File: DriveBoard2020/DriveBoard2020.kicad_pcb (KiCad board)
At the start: 2 copper layers, 124.5 x 107.4 mm, 92 parts, among them SW0 SW_SPST, SW1 SW_Push, SW2 SW_Push, SW3 SW_Push, SW4 SW_Push, SW5 SW_Push, SW6 SW_Push, SW7 SW_Push, SW8 SW_Push, SW9 SW_Push, U1 MAX_3232, U2 MAX_3232, U3 OKI, U4 TM4C129E_Launchpad, U5 MAX_3232, U6 OKI, U8 LDD-1500L

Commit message: finished schematic
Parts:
- removed Conn8: AndersonPP, MRDT_Connectors:Anderson_2_Horizontal_Side_by_Side
- Conn10: value Molex_SL_02 -> Molex_SL_04; footprint MRDT_Connectors:MOLEX_SL_02_Horizontal -> MRDT_Connectors:MOLEX_SL_04_Horizontal
- moved D22 242.8 mm to (220.1, 2.40)
- moved D23 239.8 mm to (209.9, 2.40)
- moved D20 239.3 mm to (204.9, 2.54)
- moved D15 239.2 mm to (200.0, 2.40)
- moved D21 238.2 mm to (189.6, 2.54)
- moved R24 226.6 mm to (189.6, 0.00)
- moved D12 176.3 mm to (128.7, 40.6)
- moved R26 143.4 mm to (209.9, 5.08)
- moved R23 138.0 mm to (204.9, 5.08)
- moved R10 134.2 mm to (123.6, 27.9)
- moved R25 132.3 mm to (220.1, 5.08)
- moved Conn10 130.2 mm to (242.6, 86.4)
- moved D10 128.3 mm to (128.7, 27.9)
- moved SW2 127.4 mm to (127.0, 22.9)
- moved R12 125.4 mm to (123.6, 40.6)
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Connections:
- net Net-(U4-PadPD0) renamed MISO2
- net Net-(U4-PadPD1) renamed MOSI2
- net Net-(U4-PadPD2) renamed cs2
- net Net-(U4-PadPD3) renamed clk2
- Conn10 pad 1: /Headlight_V1+ -> Net-(Conn10-Pad1)
- Conn10 pad 2: /Headlight_V1- -> Net-(Conn10-Pad2)
- U4 pad PF1: Net-(U4-PadPF1) -> Headlight_OnOff_PWM
- U4 pad PK5: Net-(U4-PadPK5) -> FL_Motor
- U4 pad PK6: Net-(U4-PadPK6) -> RL_Motor
- U4 pad PM2: Net-(U4-PadPM2) -> ML_Motor
- U8 pad 11: /Headlight_V1- -> Net-(Conn10-Pad2)
- U8 pad 12: /Headlight_V1- -> Net-(Conn10-Pad2)
- U8 pad 13: /Headlight_V1+ -> Net-(Conn10-Pad1)
- U8 pad 14: /Headlight_V1+ -> Net-(Conn10-Pad1)
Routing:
- added copper zone on B.Cu, net GND
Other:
- board outline removed

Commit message: layout progress
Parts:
- removed D15, D3, D5, D6: LED, LED_SMD:LED_0603_1608Metric_Pad1.05x0.95mm_HandSolder
- added Rx3: LED, LED_SMD:LED_0603_1608Metric_Pad1.05x0.95mm_HandSolder, F.Cu at (161.7, 85.1)
- added Tx3: LED, LED_SMD:LED_0603_1608Metric_Pad1.05x0.95mm_HandSolder, F.Cu at (165.4, 85.1)
- added Tx4: LED, LED_SMD:LED_0603_1608Metric_Pad1.05x0.95mm_HandSolder, F.Cu at (156.6, 85.1)
- added Tx7: LED, LED_SMD:LED_0603_1608Metric_Pad1.05x0.95mm_HandSolder, F.Cu at (130.2, 85.1)
- Change Direction: renamed from SW0
- Front Left Motor: renamed from SW2
- Front Right Motor: renamed from SW1
- Middle Left Motor: renamed from SW4
- Middle Right Motor: renamed from SW3
- Neopixel Pattern: renamed from SW9
- Neopixel White: renamed from SW8
- Rear Left Motor: renamed from SW6
- Rear Right Motor: renamed from SW5
- moved U2 151.7 mm to (269.9, 152.4)
- moved U5 150.8 mm to (269.9, 180.3)
- moved U1 150.2 mm to (269.9, 166.4)
- moved U6 129.1 mm to (154.9, 141.0), turned to 90 degrees
- moved C4 127.5 mm to (263.5, 170.8), turned to 90 degrees
- moved U3 124.7 mm to (154.9, 153.7), turned to 90 degrees
- moved C5 123.2 mm to (263.5, 186.1), turned to 270 degrees
- moved C6 111.7 mm to (263.5, 146.4), turned to 270 degrees
- moved C7 107.6 mm to (263.5, 151.1), turned to 270 degrees
- moved R18 107.5 mm to (130.2, 87.0)
- moved C8 104.5 mm to (263.5, 161.9), turned to 270 degrees
- moved R22 103.8 mm to (126.4, 87.0)
- moved U8 103.2 mm to (197.5, 130.8)
- moved Tx6 102.6 mm to (139.1, 85.1), turned to 0 degrees
- moved R1 102.3 mm to (139.1, 87.0), turned to 0 degrees
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- renumbered SW7 to Headlights, D23 to Rx2, D4 to Rx4, D21 to Rx5, D2 to Rx6, D19 to Rx7, D22 to Tx2, D20 to Tx5, D1 to Tx6
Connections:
- Conn1 pad 3: (no net) -> +12VA
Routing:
- net +12VA: track 0.00 -> 50.2 mm
- net +12V: track 0.00 -> 27.7 mm
- net Net-(C3-Pad1): track 0.00 -> 22.8 mm
- net Net-(C4-Pad1): track 0.00 -> 21.6 mm
- net Net-(C5-Pad1): track 0.00 -> 20.2 mm
- net Net-(C5-Pad2): track 0.00 -> 7.26 mm
- net Net-(C6-Pad2): track 0.00 -> 5.19 mm
- net Net-(C6-Pad1): track 0.00 -> 4.86 mm
- net Net-(C8-Pad2): track 0.00 -> 4.56 mm
- net Net-(C4-Pad2): track 0.00 -> 4.56 mm
- net Net-(C7-Pad1): track 0.00 -> 4.50 mm
- net Net-(C13-Pad2): track 0.00 -> 4.40 mm
- net Net-(C7-Pad2): track 0.00 -> 4.30 mm
- net Net-(C8-Pad1): track 0.00 -> 4.24 mm
- net Net-(C13-Pad1): track 0.00 -> 4.20 mm
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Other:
- board text added: "MOTORS"
- board text added: "Power Indicators"
- board text added: "Serial Indicators"

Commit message: working on traces
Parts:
- removed Change Direction: SW_SPST, Button_Switch_THT:SW_CuK_JS202011AQN_DPDT_Angled
- removed D17, D18: Org_LED, LED_SMD:LED_0603_1608Metric_Pad1.05x0.95mm_HandSolder
- removed R20, R21: 500, Resistor_SMD:R_0603_1608Metric_Pad1.05x0.95mm_HandSolder
- added Conn12: Molex_SL_05, MRDT_Connectors:MOLEX_SL_05_Horizontal, F.Cu at (136.5, 89.5)
- added SW0: SW_SPST, Button_Switch_THT:SW_CuK_JS202011CQN_DPDT_Straight, F.Cu at (168.3, 41.8)
- SW1: renamed from Front Right Motor
- SW2: renamed from Front Left Motor
- SW3: renamed from Middle Right Motor
- SW4: renamed from Middle Left Motor
- SW5: renamed from Rear Right Motor
- SW6: renamed from Rear Left Motor
- SW8: renamed from Neopixel White
- SW9: renamed from Neopixel Pattern
- moved U2 111.5 mm to (172.7, 97.8), turned to 90 degrees
- moved U1 107.8 mm to (186.7, 97.8), turned to 90 degrees
- moved U5 107.7 mm to (200.7, 97.8), turned to 90 degrees
- moved C6 105.6 mm to (166.8, 104.1), turned to 0 degrees
- moved C7 103.4 mm to (171.4, 104.1), turned to 0 degrees
- moved C3 101.6 mm to (175.9, 104.1), turned to 180 degrees
- moved C5 99.9 mm to (206.4, 104.1), turned to 0 degrees
- moved C8 99.7 mm to (182.2, 104.1), turned to 0 degrees
- moved C13 98.9 mm to (201.7, 104.1), turned to 0 degrees
- moved C11 98.9 mm to (186.7, 104.1), turned to 0 degrees
- moved C12 98.4 mm to (197.2, 104.1), turned to 0 degrees
- moved C4 98.4 mm to (191.1, 104.1), turned to 180 degrees
- moved Conn10 81.4 mm to (210.8, 137.2), turned to 180 degrees
- moved Conn5 63.4 mm to (230.6, 135.1)
- moved Conn4 44.1 mm to (230.6, 80.8), turned to 270 degrees
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- renumbered Tx6 to D1, Tx7 to D15, Rx7 to D19, Rx6 to D2, Tx5 to D20, Rx5 to D21, Tx2 to D22, Rx2 to D23, Tx4 to D3, Rx4 to D4, Tx3 to D5, Rx3 to D6, Headlights to SW7
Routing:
- net +3V3: track 0.00 -> 296.1 mm, vias 0 -> 4
- net +5V: track 0.00 -> 212.1 mm, vias 0 -> 3
- net FL_Out: track 0.00 -> 99.2 mm, vias 0 -> 1
- net FL_In: track 0.00 -> 96.2 mm, vias 0 -> 1
- net FR_In: track 0.00 -> 79.4 mm, vias 0 -> 2
- net FR_Out: track 0.00 -> 78.3 mm
- net Rx7: track 0.00 -> 76.8 mm, vias 0 -> 2
- net Tx7: track 0.00 -> 72.5 mm, vias 0 -> 2
- net Rx6: track 0.00 -> 72.2 mm, vias 0 -> 2
- net ML_Out: track 0.00 -> 70.6 mm, vias 0 -> 1
- net Rx5: track 0.00 -> 70.4 mm, vias 0 -> 2
- net Tx5: track 0.00 -> 68.8 mm, vias 0 -> 2
- net Tx6: track 0.00 -> 68.2 mm, vias 0 -> 2
- net ML_In: track 0.00 -> 66.5 mm, vias 0 -> 1
- net Rx4: track 0.00 -> 66.4 mm, vias 0 -> 2
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
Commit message: traces complete
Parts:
- moved Conn10 19.3 mm to (215.4, 156.0), turned to 270 degrees
- moved R17 5.41 mm to (179.5, 51.8)
- turned D13 to 180 degrees
- turned D14 to 180 degrees
- turned R13 to 180 degrees
- turned R14 to 180 degrees
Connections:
- U4 pad PF3: Net-(U4-PadPF3) -> FR_Motor
- U4 pad PG0: Net-(U4-PadPG0) -> FL_Motor
- U4 pad PH1: RR_Motor -> Net-(U4-PadPH1)
- U4 pad PK4: FR_Motor -> Net-(U4-PadPK4)
- U4 pad PK5: FL_Motor -> Net-(U4-PadPK5)
- U4 pad PK6: RL_Motor -> Net-(U4-PadPK6)
- U4 pad PL0: Net-(U4-PadPL0) -> ML_Motor
- U4 pad PL2: Net-(U4-PadPL2) -> RR_Motor
- U4 pad PL3: Net-(U4-PadPL3) -> RL_Motor
- U4 pad PL5: Net-(U4-PadPL5) -> MR_Motor
- U4 pad PM1: MR_Motor -> Net-(U4-PadPM1)
- U4 pad PM2: ML_Motor -> Net-(U4-PadPM2)
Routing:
- net FL_Motor: track 11.1 -> 202.3 mm, vias 0 -> 4
- net FR_Motor: track 11.1 -> 198.9 mm, vias 0 -> 4
- net Rx2: track 29.6 -> 215.2 mm, vias 0 -> 4
- net NeoPixel_White: track 11.4 -> 177.6 mm, vias 0 -> 4
- net Tx4: track 3.12 -> 166.5 mm, vias 1 -> 6
- net MR_Motor: track 11.1 -> 164.1 mm, vias 0 -> 1
- net NeoPixel_Pattern: track 0.00 -> 147.6 mm, vias 0 -> 3
- net Tx7: track 72.5 -> 211.6 mm, vias 2 -> 6
- net Headlight_Power: track 12.5 -> 151.2 mm, vias 0 -> 2
- net RR_Motor: track 0.00 -> 138.0 mm, vias 0 -> 4
- net Rx7: track 76.8 -> 214.7 mm, vias 2 -> 6
- net Rx3: track 38.3 -> 175.1 mm, vias 0 -> 4
- net Tx3: track 33.0 -> 165.6 mm, vias 0 -> 3
- net ML_Motor: track 11.1 -> 141.3 mm, vias 0 -> 1
- net Rx5: track 70.4 -> 198.0 mm, vias 2 -> 3
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
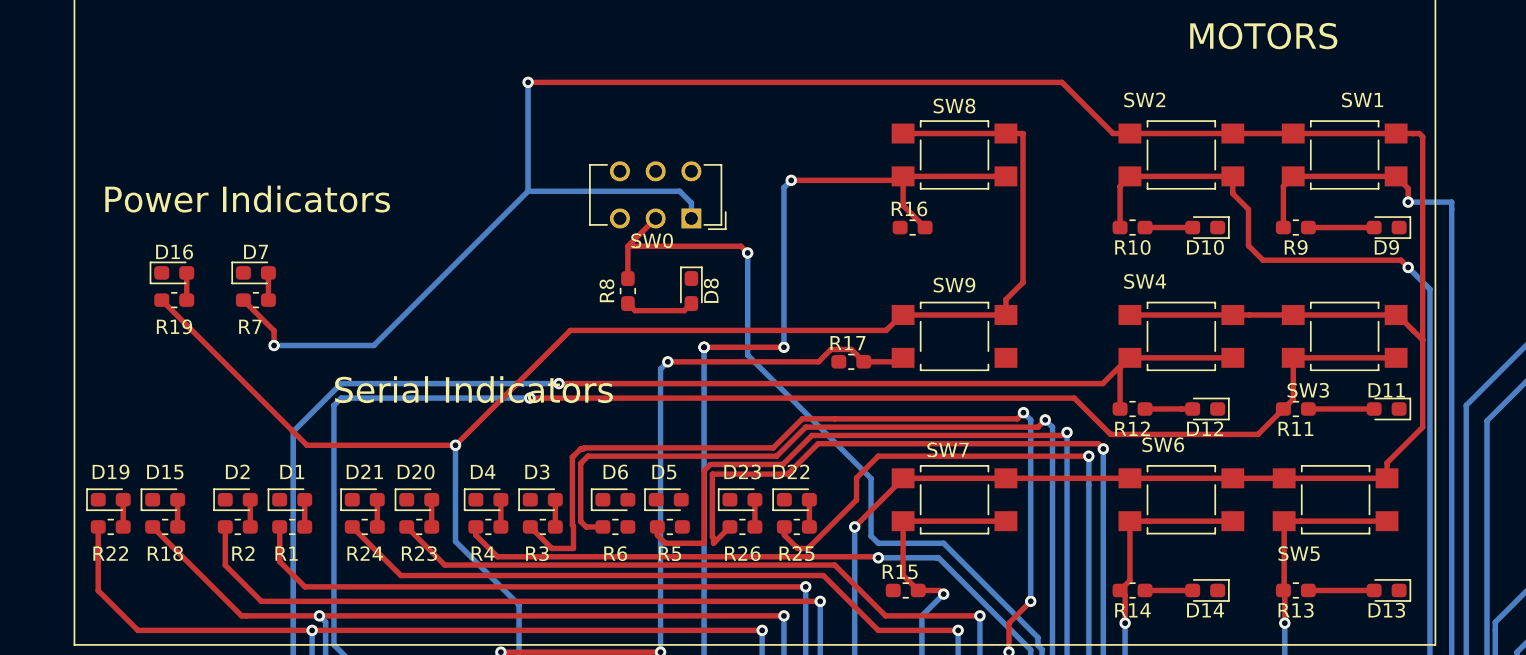
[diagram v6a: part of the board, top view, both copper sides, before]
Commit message: renamed silkscreens
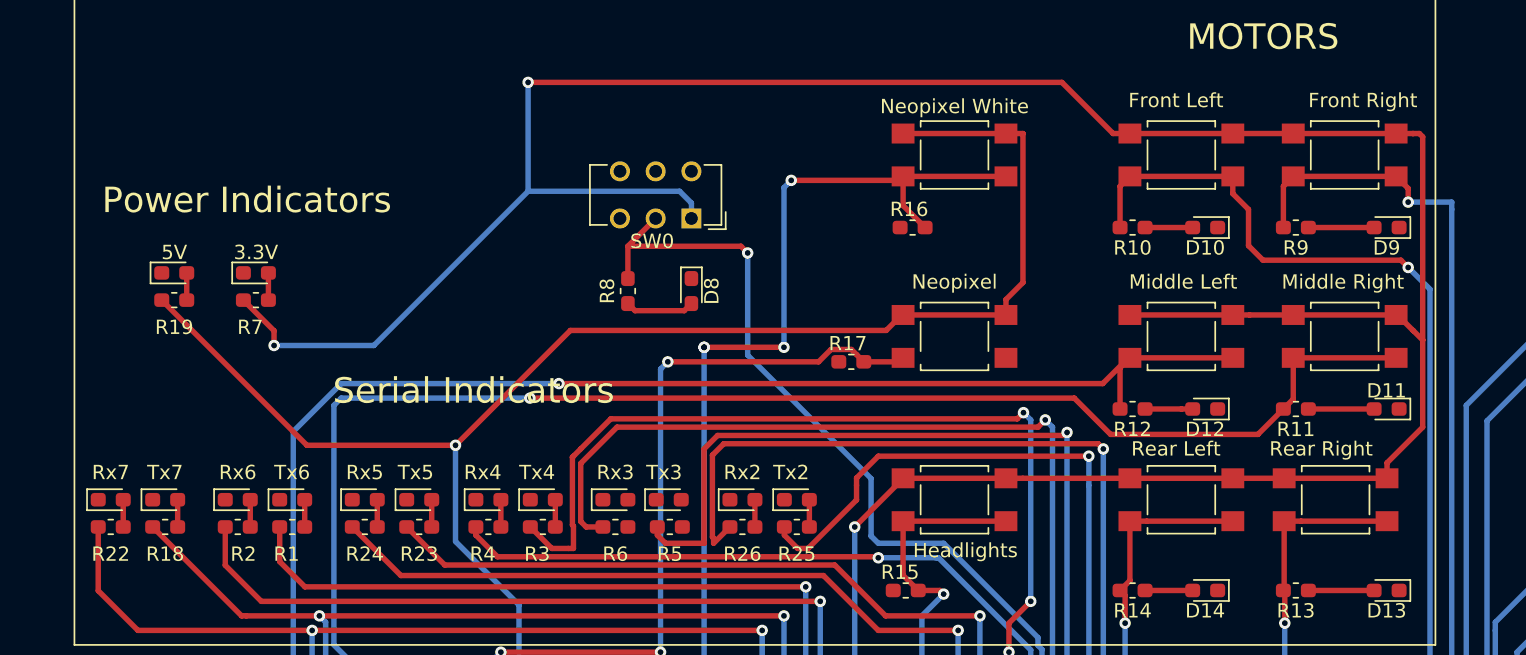
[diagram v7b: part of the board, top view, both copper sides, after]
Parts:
- Front Left: renamed from SW2
- Front Right: renamed from SW1
- Middle Left: renamed from SW4
- Middle Right: renamed from SW3
- Neopixel White: renamed from SW8
- Rear Left: renamed from SW6
- Rear Right: renamed from SW5
- renumbered D7 to 3.3V, D16 to 5V, SW7 to Headlights, SW9 to Neopixel, D23 to Rx2, D6 to Rx3, D4 to Rx4, D21 to Rx5, D2 to Rx6, D19 to Rx7, D22 to Tx2, D5 to Tx3, D3 to Tx4, D20 to Tx5, D1 to Tx6, D15 to Tx7
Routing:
- net Tx3: track 165.6 -> 166.5 mm
- net Rx2: track 215.2 -> 216.0 mm

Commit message: edgecuts, signatures
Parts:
- removed SW0: SW_SPST, Button_Switch_THT:SW_CuK_JS202011CQN_DPDT_Straight
- added Change Direction: SW_SPST, Button_Switch_THT:SW_CuK_JS202011CQN_DPDT_Straight, F.Cu at (156.6, 89.0)
- added G***: LOGO, DriveBoard_Hardware:z_sig_Jared_Sinkey_15.5mmx34.4mm, F.Cu at (193.5, 235.7)
- added G***: LOGO, DriveBoard_Hardware:z_sig_Jack_Schott_15.2mmx27mm, F.Cu at (178.8, 224.0)
- added G***: LOGO, MRDT_Silkscreens:z_sig_Sam_Thompson_Sig_20.0mmX13.1mm, F.Cu at (203.2, 226.1)
- added G***: LOGO, MRDT_Silkscreens:0_MRDT_Logo_20mm, F.Cu at (224.5, 228.6)
- moved Conn10 52.0 mm to (204.2, 206.8)
- moved Conn5 48.7 mm to (218.9, 182.4)
- moved Conn6 48.7 mm to (218.9, 164.6)
- moved R19 48.7 mm to (120.4, 94.7)
- moved R2 48.7 mm to (124.8, 110.6)
- moved R22 48.7 mm to (116.0, 110.6)
- moved R6 48.7 mm to (151.3, 110.6)
- moved R9 48.7 mm to (198.9, 89.7)
- moved 5V 48.7 mm to (120.4, 92.8)
- moved C1 48.7 mm to (134.4, 190.5)
- moved C10 48.7 mm to (134.2, 200.0)
- moved C14 48.7 mm to (137.5, 190.5)
- moved C15 48.7 mm to (145.4, 176.8)
- moved C2 48.7 mm to (161.7, 192.4)
- moved C9 48.7 mm to (134.4, 195.8)
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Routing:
- net NeoPixel_Pattern: track 147.6 -> 156.2 mm
- net Net-(Conn10-Pad2): track 49.1 -> 54.0 mm
- net Net-(Conn10-Pad1): track 63.7 -> 67.8 mm
- net GND: track 0.00 -> 3.88 mm, vias 0 -> 6
- net Net-(D5-Pad2): track 0.00 -> 1.94 mm
- net Net-(D6-Pad2): track 0.00 -> 1.91 mm
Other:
- board outline added: 125 x 175.3 mm
- board text added: "Forward"
- board text added: "Reverse"
